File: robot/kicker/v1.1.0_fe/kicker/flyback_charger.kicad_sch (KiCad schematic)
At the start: 45 parts, among them Q1 BSC0402NSATMA1, U4 LT3751

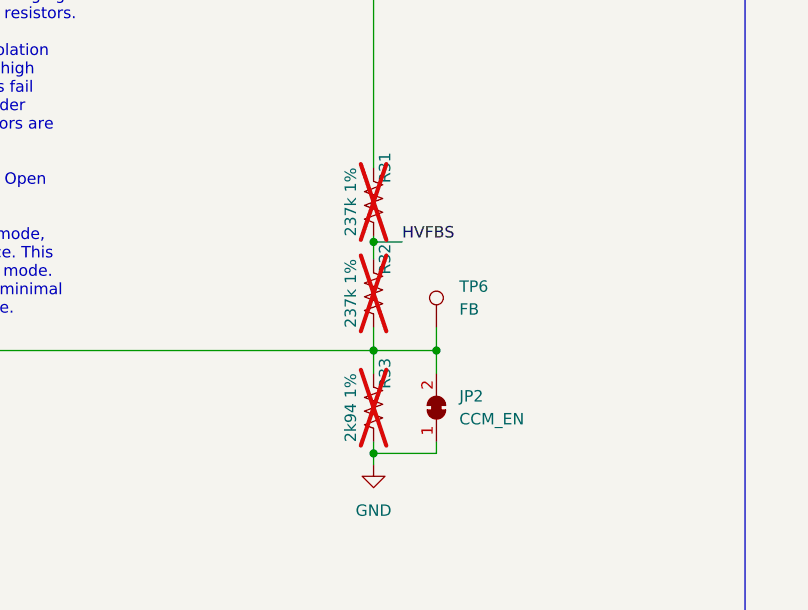
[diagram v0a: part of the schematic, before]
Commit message: NEED v7.1 DRC CHECK - change default charge mode
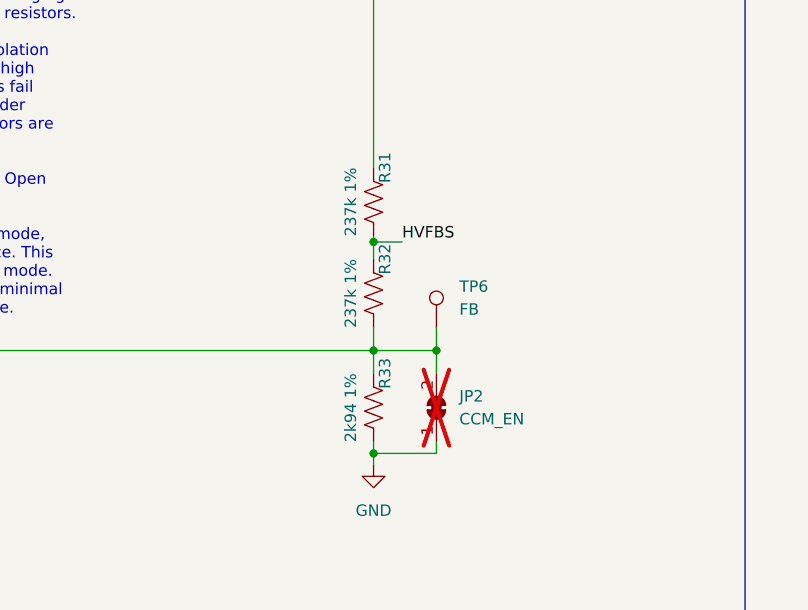
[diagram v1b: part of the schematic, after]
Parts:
- JP2: now not fitted
- R31, R32, R33: now fitted
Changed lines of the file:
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@@
   )
   (symbol (lib_id "Device:R_US") (at 358.775 192.405 180) (unit 1)
-    (in_bom yes) (on_board yes) (dnp yes)
+    (in_bom yes) (on_board yes) (dnp no)
     (property "Reference" "R31" (at 360.045 188.595 90)
       (effects (font (size 1.27 1.27)))
@@
   )
   (symbol (lib_id "Device:R_US") (at 358.775 215.265 180) (unit 1)
-    (in_bom yes) (on_board yes) (dnp yes)
+    (in_bom yes) (on_board yes) (dnp no)
     (property "Reference" "R33" (at 360.045 211.455 90)
       (effects (font (size 1.27 1.27)))
@@
   )
   (symbol (lib_id "Jumper:SolderJumper_2_Bridged") (at 365.76 215.265 90) (unit 1)
-    (in_bom yes) (on_board yes) (dnp no) (fields_autoplaced)
+    (in_bom yes) (on_board yes) (dnp yes) (fields_autoplaced)
     (property "Reference" "JP2" (at 368.3 213.9949 90)
       (effects (font (size 1.27 1.27)) (justify right))
@@
   )
   (symbol (lib_id "Device:R_US") (at 358.775 202.565 180) (unit 1)
-    (in_bom yes) (on_board yes) (dnp yes)
+    (in_bom yes) (on_board yes) (dnp no)
     (property "Reference" "R32" (at 360.045 198.755 90)
       (effects (font (size 1.27 1.27)))
